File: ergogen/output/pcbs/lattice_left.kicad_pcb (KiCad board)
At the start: 2 copper layers, 114.3 x 85.7 mm, 84 parts

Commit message: component placement
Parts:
- moved R3 15.0 mm to (145.4, 40.9)
- moved R4 15.0 mm to (145.4, 42.9)
- moved R5 15.0 mm to (145.4, 44.9)
- moved C3 9.52 mm to (171.4, 48.8)
- moved U1 3.18 mm to (155.6, 45.2)
- moved C5 2.00 mm to (183.0, 42.9)
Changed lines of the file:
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@@
         )
         (module RP2040 (layer B.Cu)
-            (at 152.4 45.243750000000006 225)
+            (at 155.57500000000002 45.243750000000006 225)
             (fp_text reference "U1" (at 0 0 0) (layer "B.Fab")
               (effects (font (size 1 1) (thickness 0.15)))
@@
         )
         (module 27R (layer B.Cu)
-            (at 160.4 40.862500000000004 0)
+            (at 145.4 40.862500000000004 0)
             (fp_text reference "R3" (at 0 0 0) (layer "B.Fab")
               (effects (font (size 1 1) (thickness 0.15)))
@@
         )
         (module 27R (layer B.Cu)
-            (at 160.4 42.862500000000004 0)
+            (at 145.4 42.862500000000004 0)
             (fp_text reference "R4" (at 0 0 0) (layer "B.Fab")
               (effects (font (size 1 1) (thickness 0.15)))
@@
         )
         (module 1k (layer B.Cu)
-            (at 160.4 44.862500000000004 0)
+            (at 145.4 44.862500000000004 0)
             (fp_text reference "R5" (at 0 0 0) (layer "B.Fab")
               (effects (font (size 1 1) (thickness 0.15)))
@@
         )
         (module 100nF (layer B.Cu)
-            (at 161.925 48.815625000000004 90)
+            (at 171.45 48.815625000000004 90)
             (fp_text reference "C3" (at 0 0 0) (layer "B.Fab")
               (effects (font (size 1 1) (thickness 0.15)))
@@
         )
         (module 22pF (layer B.Cu)
-            (at 180.975 42.862500000000004 90)
+            (at 182.975 42.862500000000004 90)
             (fp_text reference "C5" (at 0 0 0) (layer "B.Fab")
               (effects (font (size 1 1) (thickness 0.15)))

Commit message: component placement (swap crystal and flash)
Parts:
- C3: footprint 100nF -> 22pF
- C5: footprint 22pF -> 100nF
- moved C4 11.3 mm to (170.7, 47.6)
- moved Y1 9.52 mm to (166.7, 42.9)
- moved C5 6.74 mm to (178.2, 47.6)
- moved U4 6.35 mm to (174.6, 42.9)
- moved C3 3.01 mm to (168.7, 47.6)
- turned R6 to 90 degrees
- turned R7 to 90 degrees
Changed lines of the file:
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@@
+            )
+        )
+        (module 12MHz (layer B.Cu)
+            (at 166.6875 42.862500000000004 0)
+            (fp_text reference "Y1" (at 0 0 0) (layer "B.Fab")
+              (effects (font (size 1 1) (thickness 0.15)))
+            )
+        )
+        (module 1k (layer B.Cu)
+            (at 166.6875 47.62500000000001 90)
+            (fp_text reference "R6" (at 0 0 0) (layer "B.Fab")
+              (effects (font (size 1 1) (thickness 0.15)))
+            )
+        )
+        (module 22pF (layer B.Cu)
+            (at 168.6875 47.62500000000001 90)
+            (fp_text reference "C3" (at 0 0 0) (layer "B.Fab")
+              (effects (font (size 1 1) (thickness 0.15)))
+            )
+        )
+        (module 22pF (layer B.Cu)
+            (at 170.6875 47.62500000000001 90)
+            (fp_text reference "C4" (at 0 0 0) (layer "B.Fab")
+              (effects (font (size 1 1) (thickness 0.15)))
             )
         )
         (module XC6206PxxxMR (layer B.Cu)
-            (at 168.27499999999998 42.862500000000004 0)
+            (at 174.625 42.862500000000004 0)
             (fp_text reference "U4" (at 0 0 0) (layer "B.Fab")
               (effects (font (size 1 1) (thickness 0.15)))
             )
         )
-        (module 100nF (layer B.Cu)
-            (at 171.45 48.815625000000004 90)
-            (fp_text reference "C3" (at 0 0 0) (layer "B.Fab")
+        (module 1k (layer B.Cu)
+            (at 176.21249999999998 47.62500000000001 90)
+            (fp_text reference "R7" (at 0 0 0) (layer "B.Fab")
               (effects (font (size 1 1) (thickness 0.15)))
             )
         )
-        (module 1k (layer B.Cu)
-            (at 166.6875 47.62500000000001 0)
-            (fp_text reference "R6" (at 0 0 0) (layer "B.Fab")
-              (effects (font (size 1 1) (thickness 0.15)))
-            )
-        )
-        (module 12MHz (layer B.Cu)
-            (at 176.21249999999998 42.862500000000004 0)
-            (fp_text reference "Y1" (at 0 0 0) (layer "B.Fab")
-              (effects (font (size 1 1) (thickness 0.15)))
-            )
-        )
-        (module 22pF (layer B.Cu)
-            (at 180.975 42.862500000000004 90)
-            (fp_text reference "C4" (at 0 0 0) (layer "B.Fab")
-              (effects (font (size 1 1) (thickness 0.15)))
-            )
-        )
-        (module 22pF (layer B.Cu)
-            (at 182.975 42.862500000000004 90)
+        (module 100nF (layer B.Cu)
+            (at 178.21249999999998 47.62500000000001 90)
             (fp_text reference "C5" (at 0 0 0) (layer "B.Fab")
               (effects (font (size 1 1) (thickness 0.15)))
             )
-        )
-        (module 1k (layer B.Cu)
-            (at 176.21249999999998 47.62500000000001 0)
-            (fp_text reference "R7" (at 0 0 0) (layer "B.Fab")
-              (effects (font (size 1 1) (thickness 0.15)))
-            )

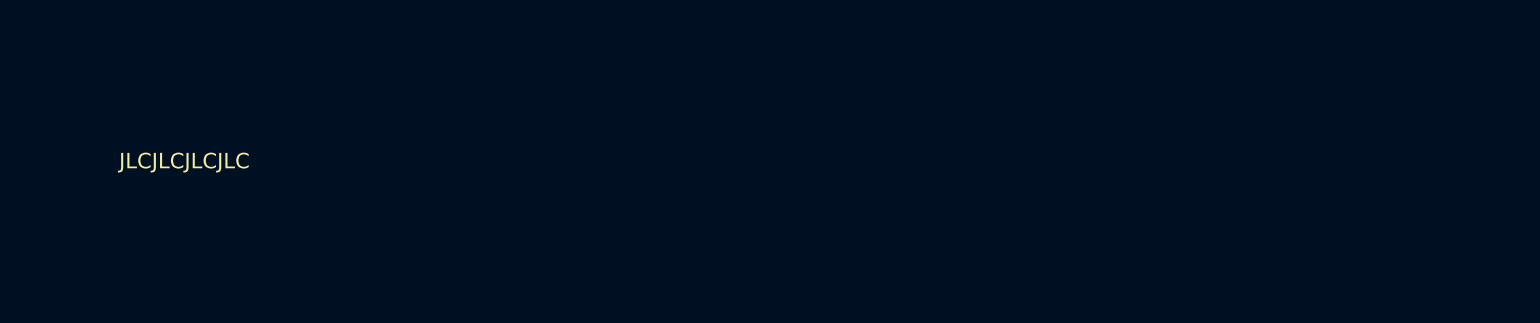
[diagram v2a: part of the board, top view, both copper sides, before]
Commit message: component placement
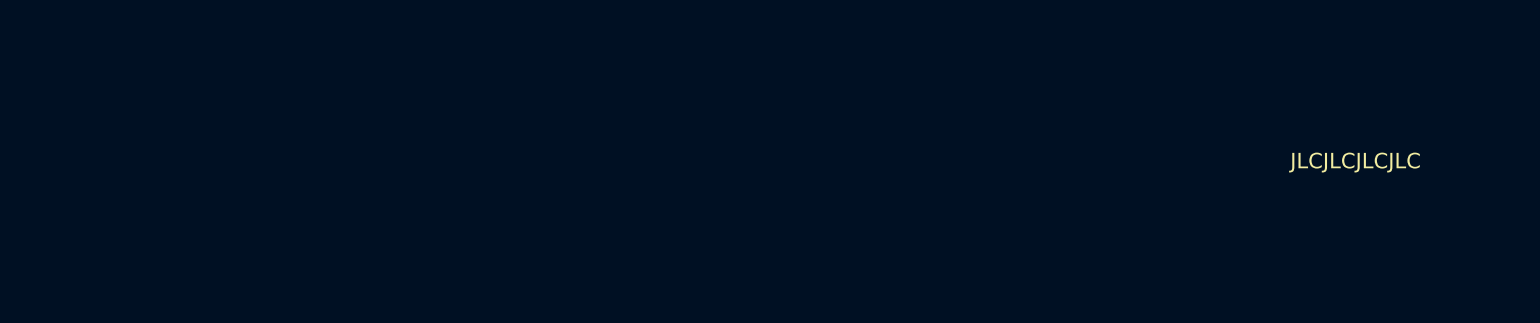
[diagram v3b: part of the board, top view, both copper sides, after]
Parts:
- removed C10, C11, C12, C13, C14, C16, C17, C8, C9: , 100nF
- removed C15, C7: , 1uF
- removed C6: , 10uF
- removed J3: , Conn_01x05
- C3: footprint 22pF -> 100nF
- C5: footprint 100nF -> 22pF
- R3, R4: footprint 27R -> 1k
- R5, R6: footprint 1k -> 27R
- U1: footprint RP2040 -> W25Q128JVS
- U2: footprint W25Q128JVS -> USBLC6-2SC6
- U3: footprint USBLC6-2SC6 -> XC6206PxxxMR
- U4: footprint XC6206PxxxMR -> RP2040
- moved R6 57.2 mm to (109.5, 47.6)
- moved C5 55.4 mm to (122.8, 47.6)
- moved C3 54.4 mm to (114.3, 49.6)
- moved U1 50.9 mm to (104.8, 42.9), turned to 270 degrees
- moved R7 48.7 mm to (127.6, 45.2), turned to 0 degrees
- moved C4 46.9 mm to (123.8, 47.6)
- moved Y1 42.9 mm to (123.8, 42.9)
- moved SYM1 42.6 mm to (181.0, 85.7)
- moved SW1 42.5 mm to (95.2, 68.2)
- moved U4 41.3 mm to (133.3, 43.6), turned to 90 degrees
- moved R5 37.0 mm to (108.5, 47.6), turned to 90 degrees
- moved SW2 35.5 mm to (114.3, 68.2)
- moved R3 31.3 mm to (115.3, 49.6), turned to 90 degrees
- moved R4 21.1 mm to (124.8, 47.6), turned to 90 degrees
- moved C2 9.77 mm to (105.8, 47.6)
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
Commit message: component placement (swap rp2040 and flash)
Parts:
- C3: footprint 100nF -> 22pF
- C5: footprint 22pF -> 100nF
- R4: footprint 1k -> 27R
- R6: footprint 27R -> 1k
- U3: footprint XC6206PxxxMR -> RP2040
- U4: footprint RP2040 -> XC6206PxxxMR
- moved R5 34.7 mm to (142.9, 42.9), turned to 0 degrees
- moved R6 33.5 mm to (142.9, 43.9), turned to 0 degrees
- moved C5 25.6 mm to (148.4, 47.6)
- moved R7 20.0 mm to (147.4, 47.6), turned to 90 degrees
- moved U4 19.1 mm to (152.4, 43.9), turned to 270 degrees
- moved R4 18.9 mm to (142.9, 41.9), turned to 0 degrees
- moved U3 17.1 mm to (133.3, 43.6), turned to 90 degrees
- moved C3 9.73 mm to (123.8, 47.6)
- moved R3 9.73 mm to (124.8, 47.6)
- moved C4 1.00 mm to (122.8, 47.6)
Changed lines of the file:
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@@
-            )
-        )
-        (module XC6206PxxxMR (layer B.Cu)
-            (at 116.3 43.862500000000004 270)
-            (fp_text reference "U3" (at 0 0 0) (layer "B.Fab")
-              (effects (font (size 1 1) (thickness 0.15)))
-            )
-        )
-        (module 1k (layer B.Cu)
-            (at 115.3 49.62500000000001 90)
-            (fp_text reference "R3" (at 0 0 0) (layer "B.Fab")
-              (effects (font (size 1 1) (thickness 0.15)))
-            )
-        )
-        (module 100nF (layer B.Cu)
-            (at 114.3 49.62500000000001 90)
-            (fp_text reference "C3" (at 0 0 0) (layer "B.Fab")
-              (effects (font (size 1 1) (thickness 0.15)))
             )
         )
@@
         (module 1k (layer B.Cu)
             (at 124.82499999999999 47.62500000000001 90)
-            (fp_text reference "R4" (at 0 0 0) (layer "B.Fab")
+            (fp_text reference "R3" (at 0 0 0) (layer "B.Fab")
               (effects (font (size 1 1) (thickness 0.15)))
             )
@@
         (module 22pF (layer B.Cu)
             (at 123.82499999999999 47.62500000000001 90)
-            (fp_text reference "C4" (at 0 0 0) (layer "B.Fab")
+            (fp_text reference "C3" (at 0 0 0) (layer "B.Fab")
               (effects (font (size 1 1) (thickness 0.15)))
             )
@@
         (module 22pF (layer B.Cu)
             (at 122.82499999999999 47.62500000000001 90)
-            (fp_text reference "C5" (at 0 0 0) (layer "B.Fab")
+            (fp_text reference "C4" (at 0 0 0) (layer "B.Fab")
               (effects (font (size 1 1) (thickness 0.15)))
             )
@@
         (module RP2040 (layer B.Cu)
             (at 133.35 43.62500000000001 90)
+            (fp_text reference "U3" (at 0 0 0) (layer "B.Fab")
+              (effects (font (size 1 1) (thickness 0.15)))
+            )
+        )
+        (module 27R (layer B.Cu)
+            (at 142.875 41.862500000000004 0)
+            (fp_text reference "R4" (at 0 0 0) (layer "B.Fab")
+              (effects (font (size 1 1) (thickness 0.15)))
+            )
+        )
+        (module 27R (layer B.Cu)
+            (at 142.875 42.862500000000004 0)
+            (fp_text reference "R5" (at 0 0 0) (layer "B.Fab")
+              (effects (font (size 1 1) (thickness 0.15)))
+            )
+        )
+        (module 1k (layer B.Cu)
+            (at 142.875 43.862500000000004 0)
+            (fp_text reference "R6" (at 0 0 0) (layer "B.Fab")
+              (effects (font (size 1 1) (thickness 0.15)))
+            )
+        )
+        (module XC6206PxxxMR (layer B.Cu)
+            (at 152.4 43.862500000000004 270)
             (fp_text reference "U4" (at 0 0 0) (layer "B.Fab")
               (effects (font (size 1 1) (thickness 0.15)))
             )
         )
-        (module 27R (layer B.Cu)
-            (at 108.5375 47.62500000000001 90)
-            (fp_text reference "R5" (at 0 0 0) (layer "B.Fab")
+        (module 1k (layer B.Cu)
+            (at 147.4 47.62500000000001 90)
+            (fp_text reference "R7" (at 0 0 0) (layer "B.Fab")
               (effects (font (size 1 1) (thickness 0.15)))
             )
         )
-        (module 27R (layer B.Cu)
-            (at 109.5375 47.62500000000001 90)
-            (fp_text reference "R6" (at 0 0 0) (layer "B.Fab")
+        (module 100nF (layer B.Cu)
+            (at 148.4 47.62500000000001 90)
+            (fp_text reference "C5" (at 0 0 0) (layer "B.Fab")
               (effects (font (size 1 1) (thickness 0.15)))
             )
-        )
-        (module 1k (layer B.Cu)
-            (at 127.58749999999999 45.243750000000006 0)
-            (fp_text reference "R7" (at 0 0 0) (layer "B.Fab")
-              (effects (font (size 1 1) (thickness 0.15)))
-            )
